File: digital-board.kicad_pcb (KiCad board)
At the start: 2 copper layers, 200 x 150 mm, 231 parts, among them IC1 ATMEGA6450-A, J1 CONN_20X2, Q1 2N3904, Q2 2N3904, SW15 TACT_SWITCH, SW16 TACT_SWITCH, SW17 TACT_SWITCH, SW18 TACT_SWITCH, SW19 TACT_SWITCH, SW20 TACT_SWITCH, SW21 TACT_SWITCH, SW22 TACT_SWITCH, SW23 TACT_SWITCH, U1 DG419, U10 74LVC1G32, U12 74AC595, U13 74AC595, U14 74HC165, U15 74AC595, U16 74AC595, U2 74HC4067, U3 R-78E5.0-1.0, U4 74HC4067, U5 74LS573, U6 74LS573, U7 74LVC2G04, U8 74AC595, U9 74HC165, X1 MIDI OUT, X2 MIDI IN, X3 MIDI THRU

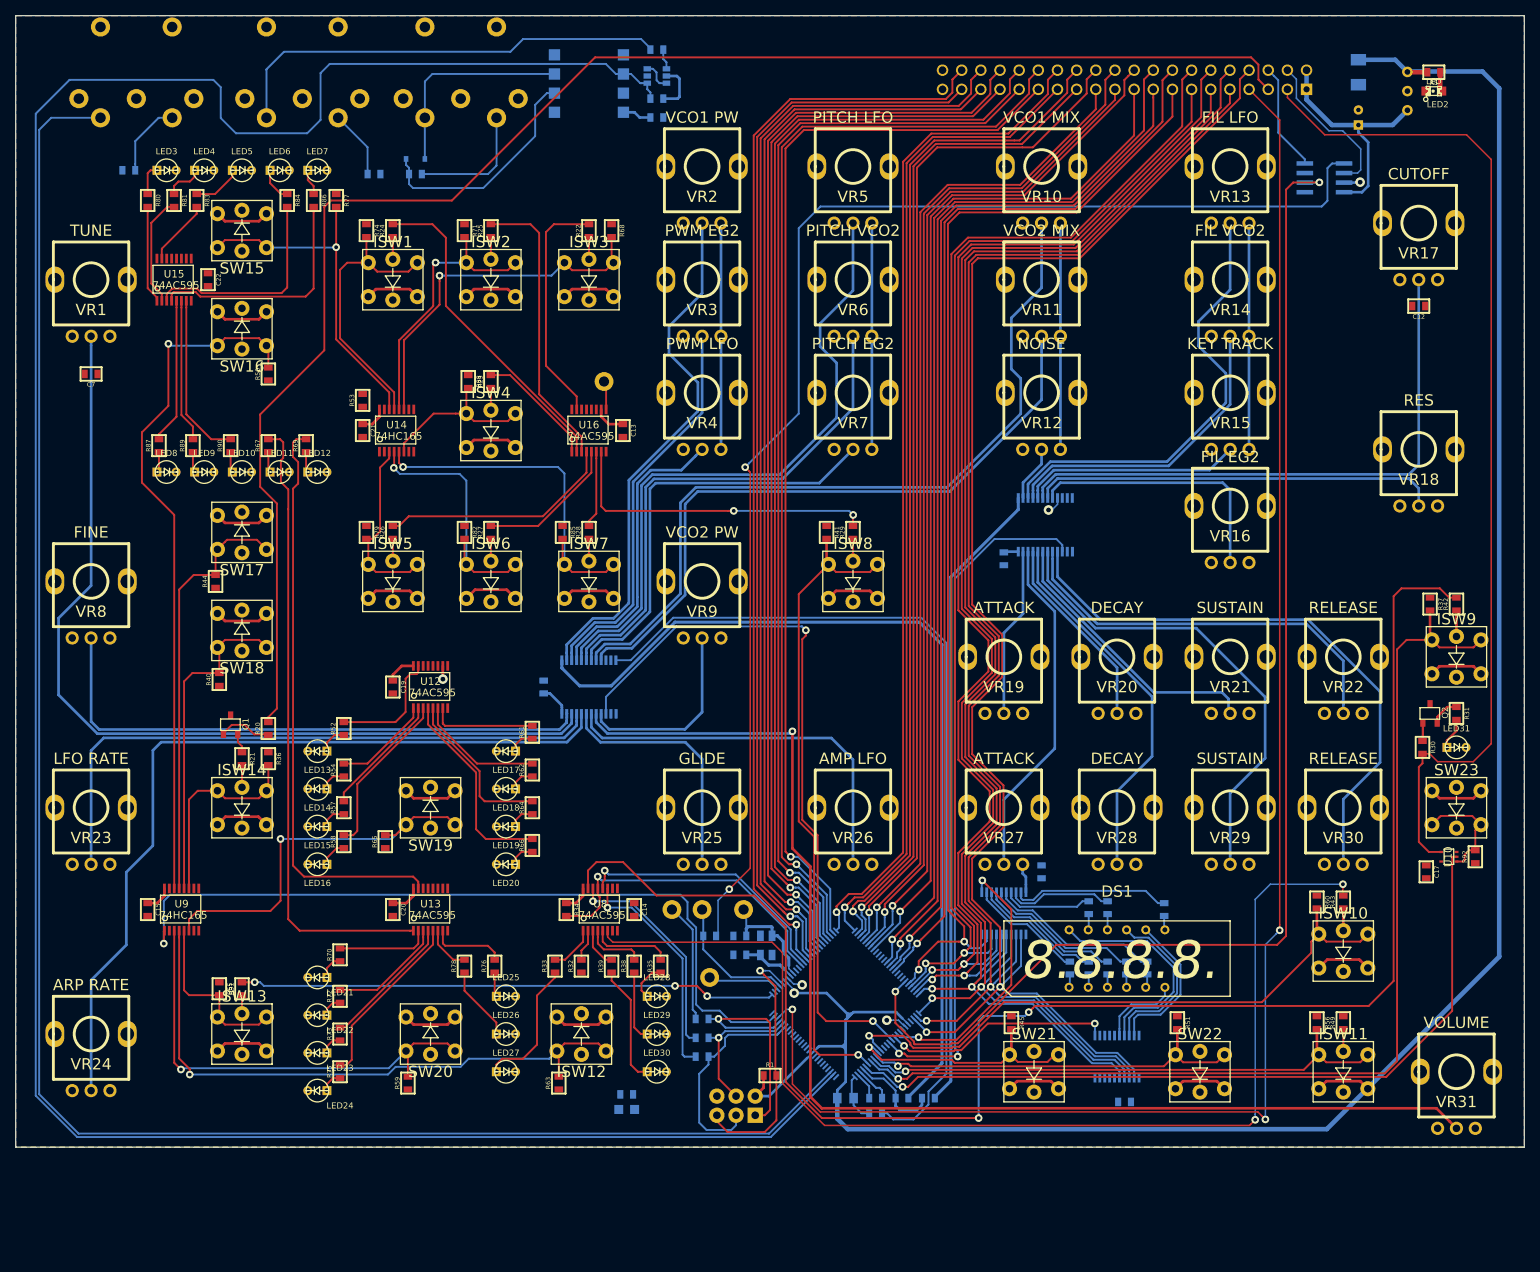
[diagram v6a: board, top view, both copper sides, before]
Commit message: routed everything but power tracks
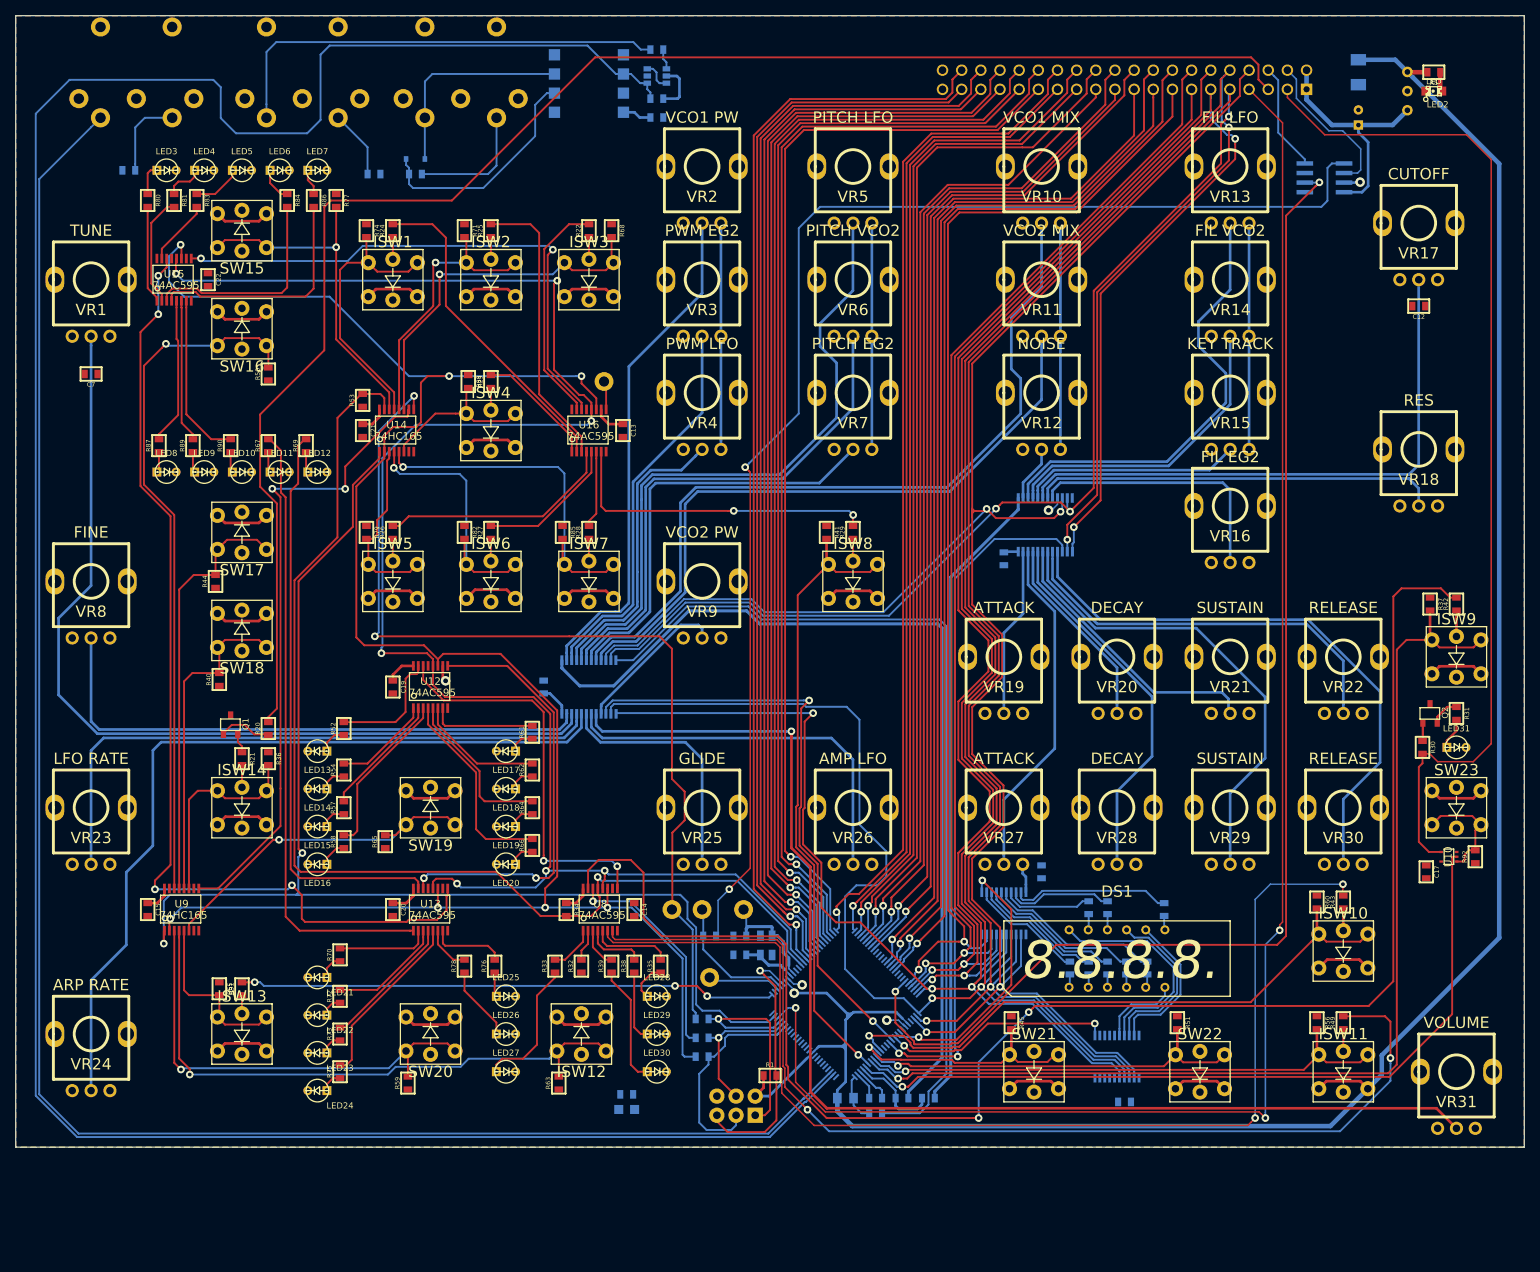
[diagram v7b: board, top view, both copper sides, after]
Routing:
- net SPI_SCK: track 29.9 -> 267.3 mm, vias 1 -> 7
- net LED_LATCH: track 35.5 -> 239.8 mm, vias 1 -> 7
- net DB2: track 194.6 -> 345.8 mm, vias 2 -> 4
- net Net-(R49-Pad2): track 0.00 -> 142.6 mm, vias 0 -> 2
- net DB3: track 190.3 -> 326.9 mm, vias 2 -> 5
- net Net-(U13-Pad9): track 0.00 -> 133.9 mm, vias 0 -> 4
- net DB1: track 193.6 -> 324.3 mm, vias 2 -> 5
- net SPI_MISO: track 15.9 -> 127.7 mm, vias 0 -> 2
- net ~SPI_EN: track 42.5 -> 152.2 mm
- net Net-(U14-Pad10): track 0.00 -> 84.1 mm, vias 0 -> 2
- net Net-(U15-Pad9): track 0.00 -> 72.5 mm, vias 0 -> 2
- net DB0: track 199.2 -> 267.8 mm, vias 2 -> 4
- net SWITCH_LATCH: track 103.5 -> 167.9 mm, vias 1 -> 2
- net Net-(U12-Pad9): track 0.00 -> 57.2 mm, vias 0 -> 2
- net Net-(U12-Pad14): track 0.00 -> 52.3 mm, vias 0 -> 2
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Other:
- net class POWER: trace_width 0.3556 -> 0.254

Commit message: finished routing and ground stitching
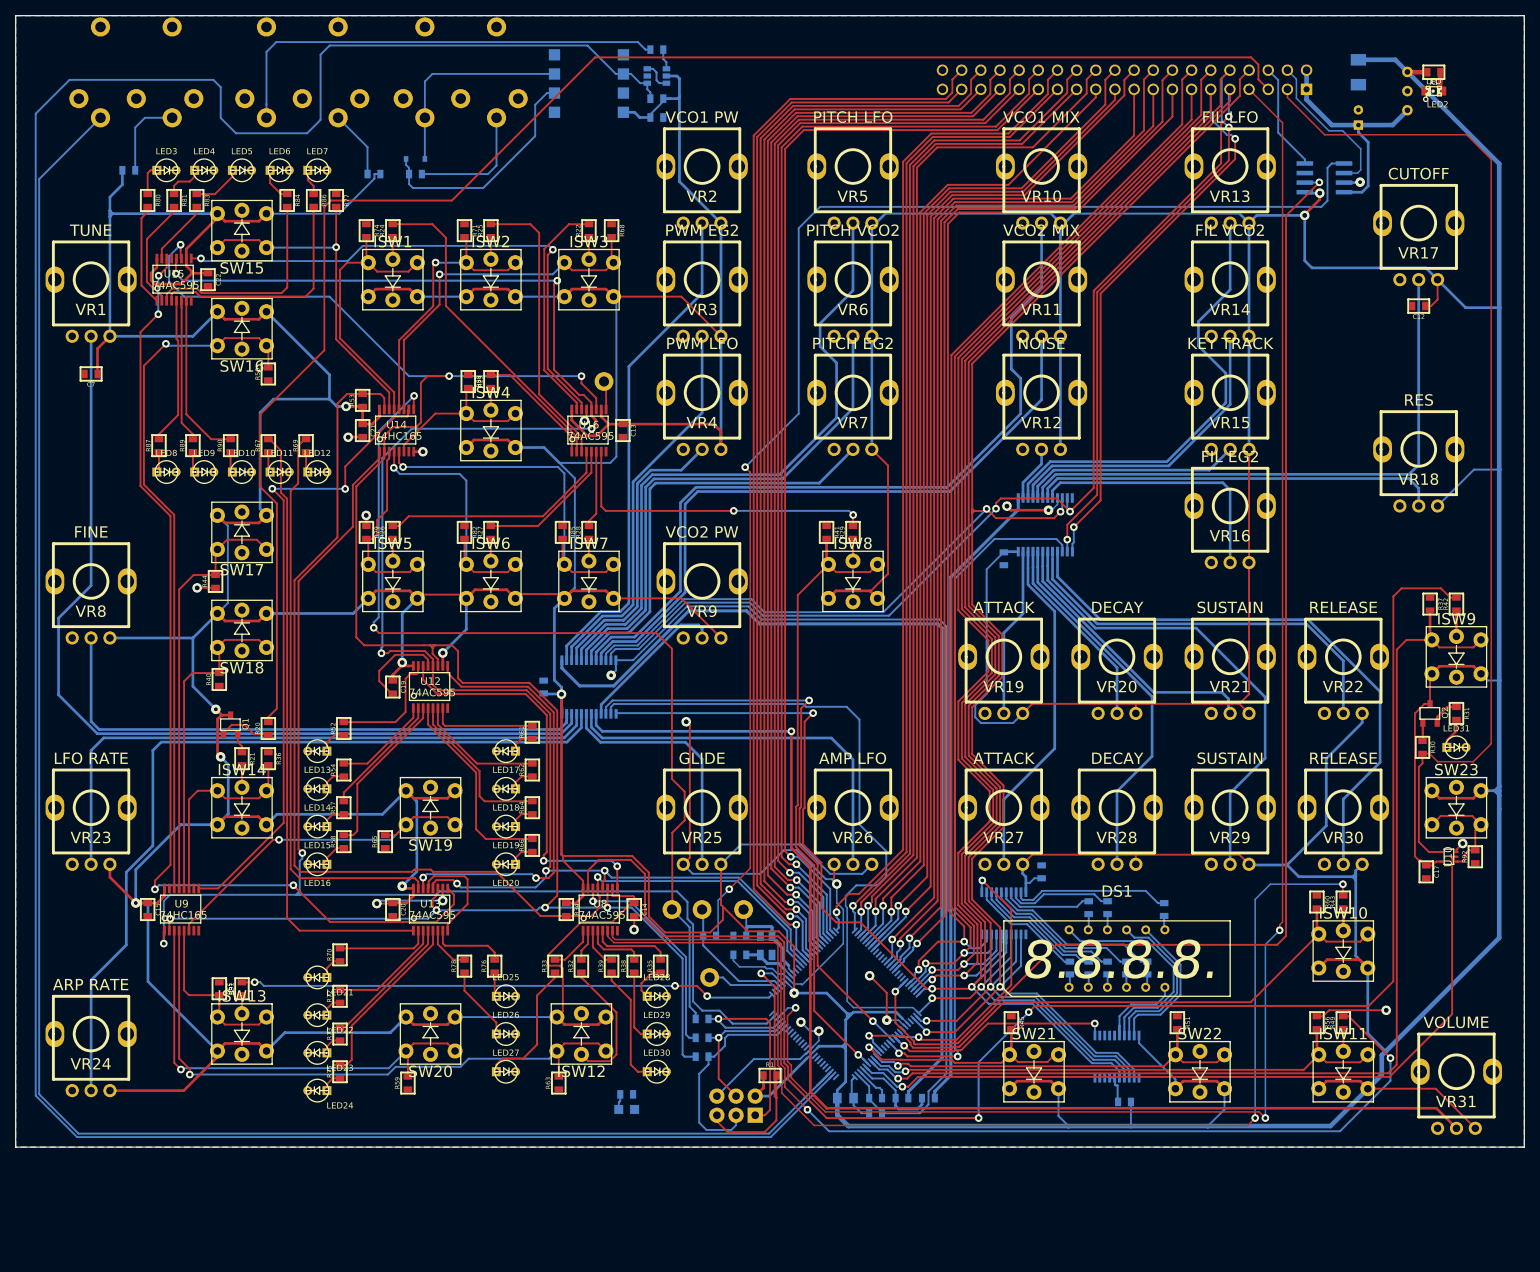
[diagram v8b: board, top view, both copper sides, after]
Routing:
- net +5V: track 617.5 -> 1728.5 mm, vias 2 -> 13
- net GND: track 131.8 -> 293.6 mm, vias 4 -> 18
- net Net-(ISW12-Pad6): track 0.00 -> 18.2 mm
- net SPI_SCK: track 267.3 -> 272.7 mm
- net DB2: track 345.8 -> 349.1 mm
- net Net-(R49-Pad2): track 142.6 -> 139.8 mm
- net /DAC12: track 132.7 -> 135.3 mm
- net UART TX: track 243.3 -> 245.8 mm
- net ~RESET: track 34.4 -> 36.6 mm
- net Net-(U4-Pad22): track 45.7 -> 47.9 mm
- net DB3: track 326.9 -> 329.0 mm
- net Net-(U4-Pad21): track 26.1 -> 28.2 mm
- net Net-(LED1-Pad1): track 0.00 -> 2.10 mm
- net Net-(U4-Pad20): track 49.6 -> 51.7 mm
- net Net-(U4-Pad19): track 37.0 -> 39.0 mm
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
